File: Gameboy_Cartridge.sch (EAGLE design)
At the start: 5 parts, among them IC1 AT49F040J

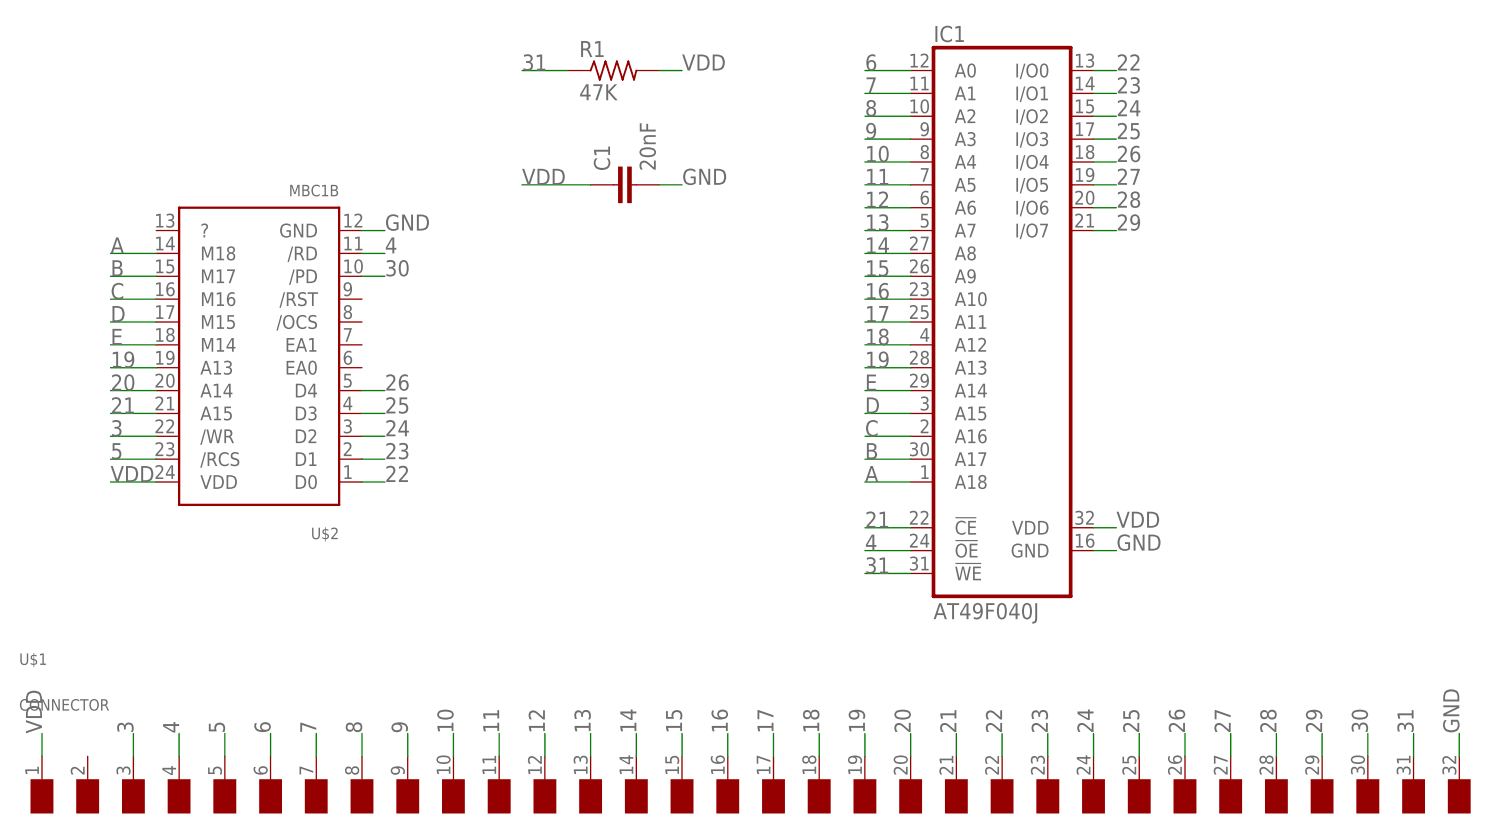
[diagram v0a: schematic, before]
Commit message: remove old chips and routing
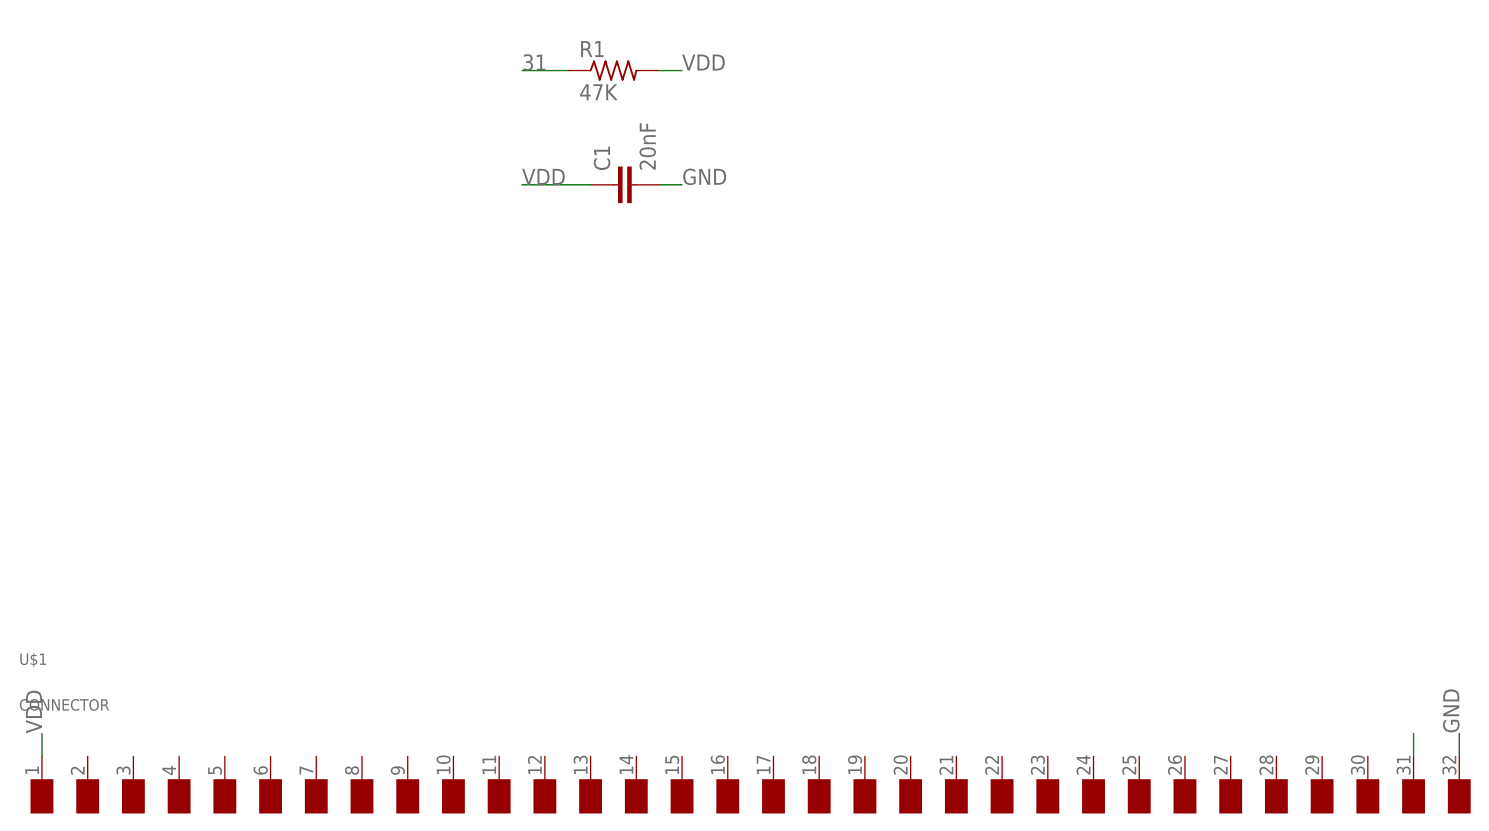
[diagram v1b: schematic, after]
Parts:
- removed IC1: AT49F040J, gameboy:AT49F040J
- removed U$2: MBC1B, gameboy:MBC1B
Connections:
- removed net 10: IC1.A4, U$1.A4
- removed net 11: IC1.A5, U$1.A5
- removed net 12: IC1.A6, U$1.A6
- removed net 13: IC1.A7, U$1.A7
- removed net 14: IC1.A8, U$1.A8
- removed net 15: IC1.A9, U$1.A9
- removed net 16: IC1.A10, U$1.A10
- removed net 17: IC1.A11, U$1.A11
- removed net 18: IC1.A12, U$1.A12
- removed net 19: IC1.A13, U$1.A13, U$2.A13
- removed net 20: U$1.A14, U$2.A14
- removed net 21: IC1.!CE, U$1.A15, U$2.A15
- removed net 22: IC1.I/O0, U$1.D0, U$2.D0
- removed net 23: IC1.I/O1, U$1.D1, U$2.D1
- removed net 24: IC1.I/O2, U$1.D2, U$2.D2
- removed net 25: IC1.I/O3, U$1.D3, U$2.D3
- removed net 26: IC1.I/O4, U$1.D4, U$2.D4
- removed net 27: IC1.I/O5, U$1.D5
- removed net 28: IC1.I/O6, U$1.D6
- removed net 29: IC1.I/O7, U$1.D7
- removed net 3: U$1./WR, U$2./WR
- removed net 30: U$1./RS, U$2./PD
- removed net 4: IC1.!OE, U$1./RD, U$2./RD
- removed net 5: U$1./RCS, U$2./RCS
- removed net 6: IC1.A0, U$1.A0
- removed net 7: IC1.A1, U$1.A1
- removed net 8: IC1.A2, U$1.A2
- removed net 9: IC1.A3, U$1.A3
- removed net A: IC1.A18, U$2.M18
- removed net B: IC1.A17, U$2.M17
- removed net C: IC1.A16, U$2.M16
- removed net D: IC1.A15, U$2.M15
- removed net E: IC1.A14, U$2.M14
- net 31: no longer IC1.!WE
- net GND: no longer IC1.GND, U$2.GND
- net VDD: no longer IC1.VDD, U$2.VDD
